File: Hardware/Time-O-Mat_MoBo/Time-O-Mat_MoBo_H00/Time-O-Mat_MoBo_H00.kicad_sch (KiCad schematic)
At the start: 37 parts, among them J1 Conn_02x04_Odd_Even, J2 Conn_02x04_Odd_Even, J3 Conn_02x04_Odd_Even, J4 Conn_02x04_Odd_Even, J5 Conn_02x04_Odd_Even, J6 Conn_01x06_Male, Q1 2N7002, SW1 SW_SPST, SW2 SW_SPST, SW3 SW_SPST, U1 ESP32-WROOM-32D, U2 DS18B20, U3 DS1302ZN+, Y1 Crystal_GND2

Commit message: HW update
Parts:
- removed G1: LOGO, 0Logo:Coufal_elektronika_text_30x13mm, symbol Graphic:SYM_Flash_Small
- removed G2: LOGO, Sergej_Library:Vedatori_15mm, symbol Graphic:SYM_Flash_Small
- added H5, H6: MountingHole, MountingHole:MountingHole_3.2mm_M3, symbol Mechanical:MountingHole
- added J8: Conn_01x03, Connector_PinHeader_2.54mm:PinHeader_1x03_P2.54mm_Vertical, symbol Connector_Generic:Conn_01x03
- added Q4: 2N7002, Package_TO_SOT_SMD:SOT-23, symbol Transistor_FET:2N7002
- added R13, R15, R16, R17: 10K, Resistor_SMD:R_0603_1608Metric, symbol Device:R
- added R14: R_Photo, OptoDevice:R_LDR_5.1x4.3mm_P3.4mm_Vertical, symbol Device:R_Photo
- C10: value Supercap 0F22 -> Supercap; footprint (none) -> Capacitor_THT:CP_Radial_D6.3mm_P2.50mm
- C8, C9: footprint (none) -> Capacitor_SMD:C_0603_1608Metric
- J6: footprint (none) -> Connector_PinHeader_2.54mm:PinHeader_1x06_P2.54mm_Vertical
- R12: renamed from R?; footprint (none) -> OptoDevice:R_LDR_5.1x4.3mm_P3.4mm_Vertical
- R3: footprint (none) -> Resistor_SMD:R_0603_1608Metric
- U2: footprint Package_TO_SOT_THT:TO-92_Inline -> Package_TO_SOT_THT:TO-92_HandSolder
- Y1: footprint (none) -> Crystal:Crystal_DS26_D2.0mm_L6.0mm_Horizontal_1EP_style2
- gave numbers to parts that had none: 2
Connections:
- net +3V3: now also R12.1, Q4.1 (G), R14.1, R16.1
- net +5V: now also J8.1 (Pin_1), R17.1
- net CE: now also U1.16 (IO13); no longer U1.11 (IO26)
- net GND: now also J8.3 (Pin_3), R13.2, R15.2
- net WS2812: now also Q4.3 (D), R17.2; no longer U1.27 (IO16)
- net LIGHT1: now reaches R12.2
- net LIGHT1: now also U1.7 (IO35), R13.1
- net at J5.5 (Pin_5), J5.6 (Pin_6): now also J8.2 (Pin_2)
- net LIGHT2: now reaches U1.6 (IO34)
- net LIGHT2: now also R14.2, R15.1
- new net: Q4.2 (S), R16.2, U1.27 (IO16)
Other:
- note added: "JUWT1105MCD"
- moved on the sheet: J1, J2, J3, J4, J5, R12

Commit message: HW updates
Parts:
- Y1: symbol Device:Crystal_GND2 -> Device:Crystal_GND3
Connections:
- net GND: now also Y1.3; no longer Y1.2
- net at C9.1, U3.3 (X2): now also Y1.2; no longer Y1.3
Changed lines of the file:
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@@
     (pin "1")
   )
-  (symbol (lib_id "Device:Crystal_GND2") (at 228.6 147.32 0) (unit 1)
+  (symbol (lib_id "Device:Crystal_GND3") (at 228.6 147.32 0) (unit 1)
     (in_bom yes) (on_board yes) (fields_autoplaced)
     (property "Reference" "Y1" (id 0) (at 228.6 140.7881 0))

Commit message: HW updates.
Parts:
- added G1: CoufalElektronika_logo, Time-O-Mat_Library:Coufal_elektronika_text_30x13mm, symbol Time-O-Mat_Library:CoufalElektronika_logo
- added G2: Vedatori_logo, Time-O-Mat_Library:Vedatori_copper_exposed_15mm, symbol Time-O-Mat_Library:Vedatori_logo
- added G3: Vedatori_logo, Time-O-Mat_Library:Vedatori_15mm, symbol Time-O-Mat_Library:Vedatori_logo
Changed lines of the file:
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@@
     (pin "1")
+  )
+  (symbol (lib_id "Time-O-Mat_Library:Vedatori_logo") (at 251.46 173.99 0) (unit 1)
+    (in_bom yes) (on_board yes) (fields_autoplaced)
+    (property "Reference" "G2" (id 0) (at 251.46 170.627 0)
+      (effects (font (size 1.27 1.27)) hide)
+    )
+    (property "Value" "Vedatori_logo" (id 1) (at 251.46 177.353 0)
+      (effects (font (size 1.27 1.27)) hide)
+    )
+    (property "Footprint" "Time-O-Mat_Library:Vedatori_copper_exposed_15mm" (id 2) (at 251.46 173.99 0)
+      (effects (font (size 1.27 1.27)) hide)
+    )
+    (property "Datasheet" "" (id 3) (at 251.46 173.99 0)
+      (effects (font (size 1.27 1.27)) hide)
+    )
   )
   (symbol (lib_id "power:+5V") (at 20.32 165.1 0) (unit 1)
@@
     (pin "1")
   )
+  (symbol (lib_id "Time-O-Mat_Library:Vedatori_logo") (at 270.51 173.99 0) (unit 1)
+    (in_bom yes) (on_board yes) (fields_autoplaced)
+    (property "Reference" "G3" (id 0) (at 270.51 170.627 0)
+      (effects (font (size 1.27 1.27)) hide)
+    )
+    (property "Value" "Vedatori_logo" (id 1) (at 270.51 177.353 0)
+      (effects (font (size 1.27 1.27)) hide)
+    )
+    (property "Footprint" "Time-O-Mat_Library:Vedatori_15mm" (id 2) (at 270.51 173.99 0)
+      (effects (font (size 1.27 1.27)) hide)
+    )
+    (property "Datasheet" "" (id 3) (at 270.51 173.99 0)
+      (effects (font (size 1.27 1.27)) hide)
+    )
+  )
   (symbol (lib_id "Device:C") (at 109.22 185.42 180) (unit 1)
     (in_bom yes) (on_board yes)
@@
     )
     (pin "1")
+  )
+  (symbol (lib_id "Time-O-Mat_Library:CoufalElektronika_logo") (at 223.52 173.99 0) (unit 1)
+    (in_bom yes) (on_board yes) (fields_autoplaced)
+    (property "Reference" "G1" (id 0) (at 223.52 167.1288 0)
+      (effects (font (size 1.27 1.27)) hide)
+    )
+    (property "Value" "CoufalElektronika_logo" (id 1) (at 223.52 180.8512 0)
+      (effects (font (size 1.27 1.27)) hide)
+    )
+    (property "Footprint" "Time-O-Mat_Library:Coufal_elektronika_text_30x13mm" (id 2) (at 223.52 173.99 0)
+      (effects (font (size 1.27 1.27)) hide)
+    )
+    (property "Datasheet" "" (id 3) (at 223.52 173.99 0)
+      (effects (font (size 1.27 1.27)) hide)
+    )
   )
   (symbol (lib_id "power:GND") (at 142.24 187.96 0) (unit 1)
@@
       (reference "D2") (unit 1) (value "B5819W") (footprint "Diode_SMD:D_SOD-123")
     )
+    (path "/d6a0720b-f931-45b4-b09d-7af773a96416"
+      (reference "G1") (unit 1) (value "CoufalElektronika_logo") (footprint "Time-O-Mat_Library:Coufal_elektronika_text_30x13mm")
+    )
+    (path "/5a951968-bff5-4e4f-a1c5-aecb7e0f59ce"
+      (reference "G2") (unit 1) (value "Vedatori_logo") (footprint "Time-O-Mat_Library:Vedatori_copper_exposed_15mm")
+    )
+    (path "/bd9ed7b6-bdd9-40c0-95f6-21b0d28d4032"
+      (reference "G3") (unit 1) (value "Vedatori_logo") (footprint "Time-O-Mat_Library:Vedatori_15mm")
+    )
     (path "/9166ea7b-5cf9-4faf-8e58-cdcf7a4c35af"

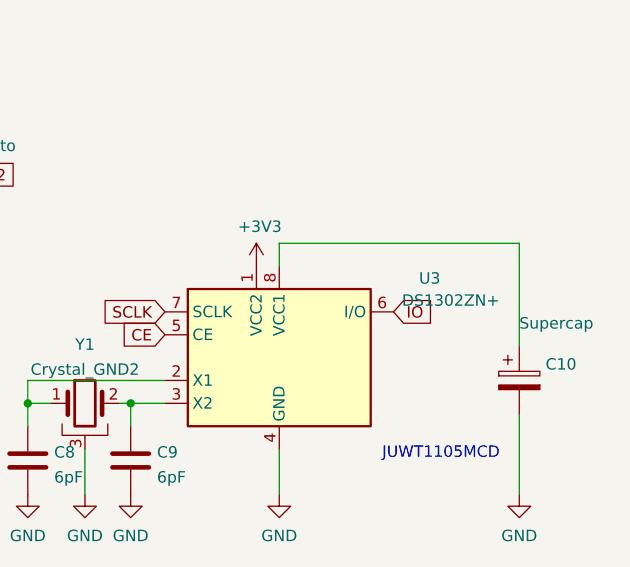
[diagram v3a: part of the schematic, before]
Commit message: Exported up to date STEP models and manufacturing data
Exported up to date 3D models of all PCB parts.
Created new subpanels fot manufacturing to counteract duplicit designators on different boards.
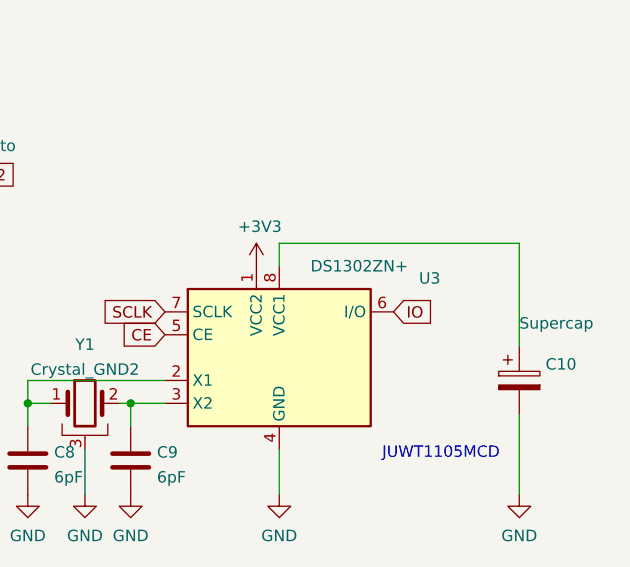
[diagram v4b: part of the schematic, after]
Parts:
- C8, C9: LCSC (none) -> C37474
- R3: LCSC (none) -> C23162
- U3: LCSC (none) -> C910859
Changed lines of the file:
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@@
+      (effects (font (size 1.27 1.27)) hide)
+    )
+    (property "LCSC" "C37474" (id 4) (at 233.68 153.67 0)
       (effects (font (size 1.27 1.27)) hide)
     )
@@
     (in_bom yes) (on_board yes)
     (property "Reference" "U3" (id 0) (at 266.9064 133.4348 0))
-    (property "Value" "DS1302ZN+" (id 1) (at 269.24 135.89 0))
+    (property "Value" "DS1302ZN+" (id 1) (at 259.08 132.08 0))
     (property "Footprint" "Package_SO:SOIC-8_3.9x4.9mm_P1.27mm" (id 2) (at 250.19 154.94 0)
       (effects (font (size 1.27 1.27)) hide)
     )
     (property "Datasheet" "https://datasheets.maximintegrated.com/en/ds/DS1302.pdf" (id 3) (at 250.19 142.24 0)
+      (effects (font (size 1.27 1.27)) hide)
+    )
+    (property "LCSC" "C910859" (id 4) (at 250.19 142.24 0)
       (effects (font (size 1.27 1.27)) hide)
     )
@@
     )
     (property "Datasheet" "~" (id 3) (at 166.37 146.05 0)
+      (effects (font (size 1.27 1.27)) hide)
+    )
+    (property "LCSC" "C23162" (id 4) (at 166.37 146.05 0)
       (effects (font (size 1.27 1.27)) hide)
     )
@@
       (effects (font (size 1.27 1.27)) hide)
     )
+    (property "LCSC" "C37474" (id 4) (at 222.25 153.67 0)
+      (effects (font (size 1.27 1.27)) hide)
+    )
     (pin "1")
     (pin "2")
@@
     )
     (path "/4ec8e228-d742-4cd8-8c0d-36879b06f45c/24ccdcff-1cb3-438a-a65b-22fe77f0a8e4"
-      (reference "J7") (unit 1) (value "TYPE-C-31-M-12") (footprint "Connector_USB:USB_C_Receptacle_HRO_TYPE-C-31-M-12")
+      (reference "J7") (unit 1) (value "918-418K2023S40001") (footprint "Connector_USB:USB_C_Receptacle_HRO_TYPE-C-31-M-12")
     )
     (path "/0fcb3a6c-41dd-4af8-b0b4-35f98e759795"
